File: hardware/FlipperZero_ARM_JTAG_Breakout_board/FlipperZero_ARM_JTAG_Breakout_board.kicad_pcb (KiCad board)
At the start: 2 copper layers, 64.5 x 36.8 mm, 23 parts, among them J1 ARM-JTAG, J10 nTRST_EN, J2 TC2050-IDC, J3 1.27mm, J4 TC2030-IDC, J5 SPI/ISP, J6 UART, J7 VTrefSel, J8 PWRSel, J9 RSTSel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

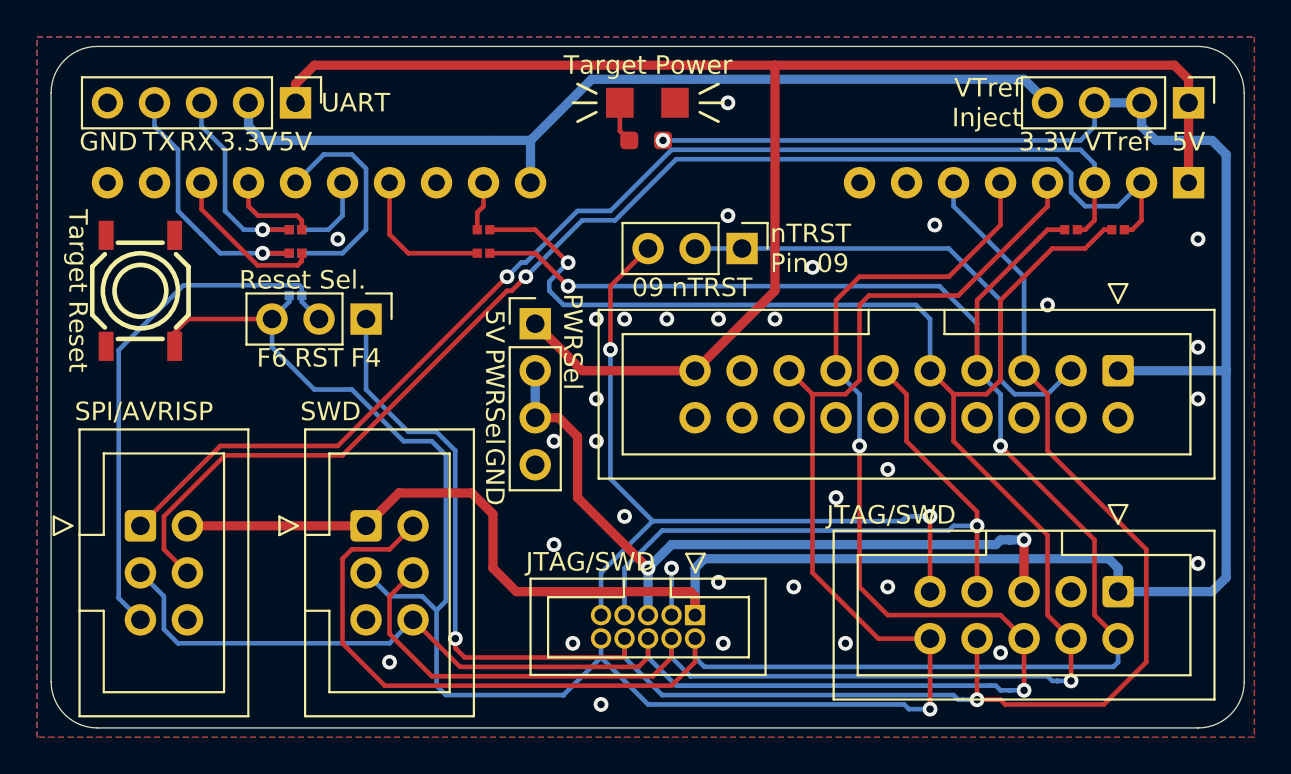
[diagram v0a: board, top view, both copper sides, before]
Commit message: added OSHW footprint template
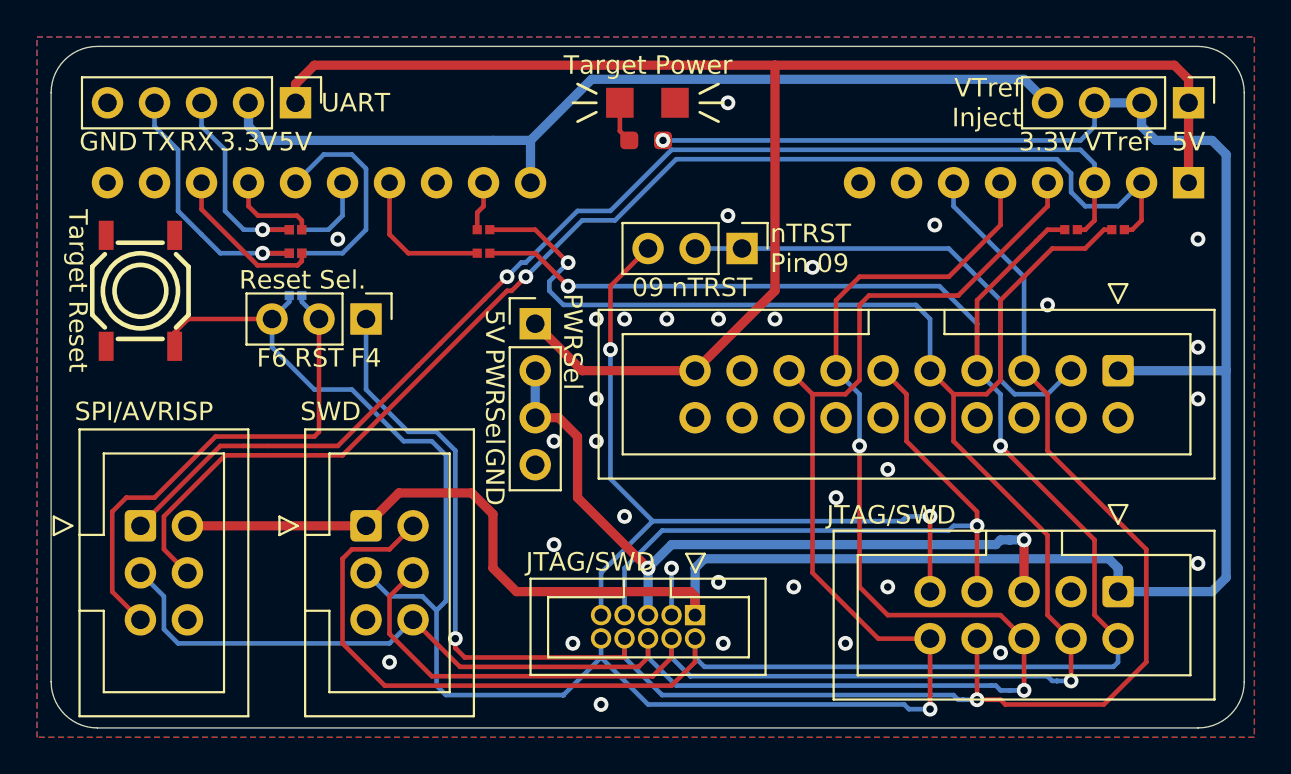
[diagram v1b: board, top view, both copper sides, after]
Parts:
- added LOGO1: ~, OSHW:OSHW-Certification-Mark-Stacked_8x7mm_SilkMask, B.Cu at (118.6, 108.2)
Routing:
- net /RSTSel: track 28.5 -> 27.2 mm
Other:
- board text removed: "FlipperZero JTAG/SWD/SPI Adapter"

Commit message: updated signal names for up-to-date terminology
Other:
- board text added: "SDI"
- board text added: "SDO"
- board text removed: "MISO"
- board text removed: "MOSI"

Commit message: updated footprint & ran DRU check
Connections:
- net /MISO renamed /SDI
- net /MOSI renamed /SDO

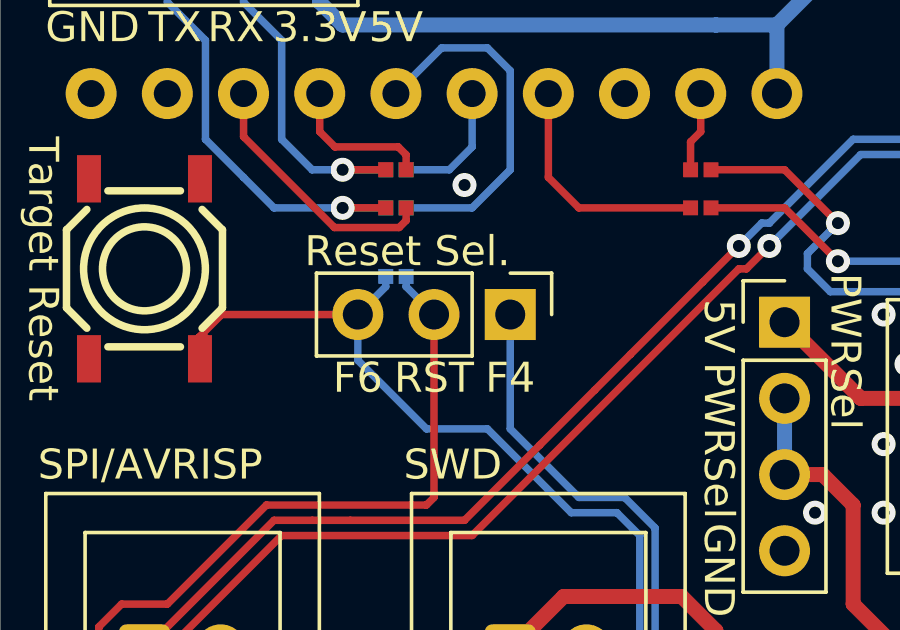
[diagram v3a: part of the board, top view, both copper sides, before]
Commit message: added jumpers on 3D models, fixed silkscreen names
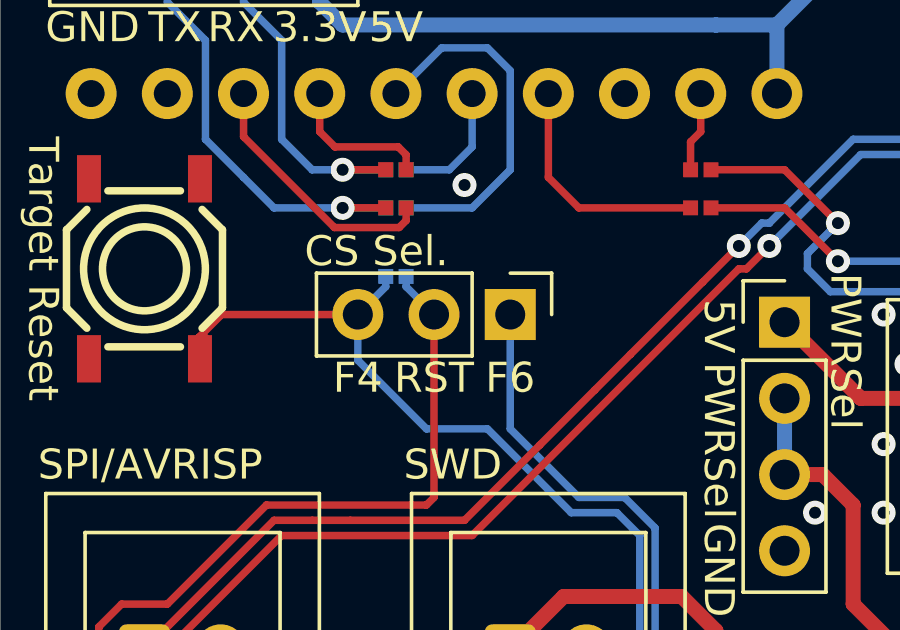
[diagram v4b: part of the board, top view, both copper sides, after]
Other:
- board text added: "CS Sel."
- board text removed: "Reset Sel."
